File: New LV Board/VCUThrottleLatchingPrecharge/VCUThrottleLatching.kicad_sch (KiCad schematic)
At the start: 30 parts, among them J1 B12B-PH-K-S:JST_B12B-PH-K-S, Q1 SS8550, U1 IRLML2060TRPBF, U2 IRLML2060TRPBF, U3 IRLML2060TRPBF, U5 IRLML2060TRPBF, U6 IRLML2060TRPBF, U8 PMV160UP, U9 NE555D

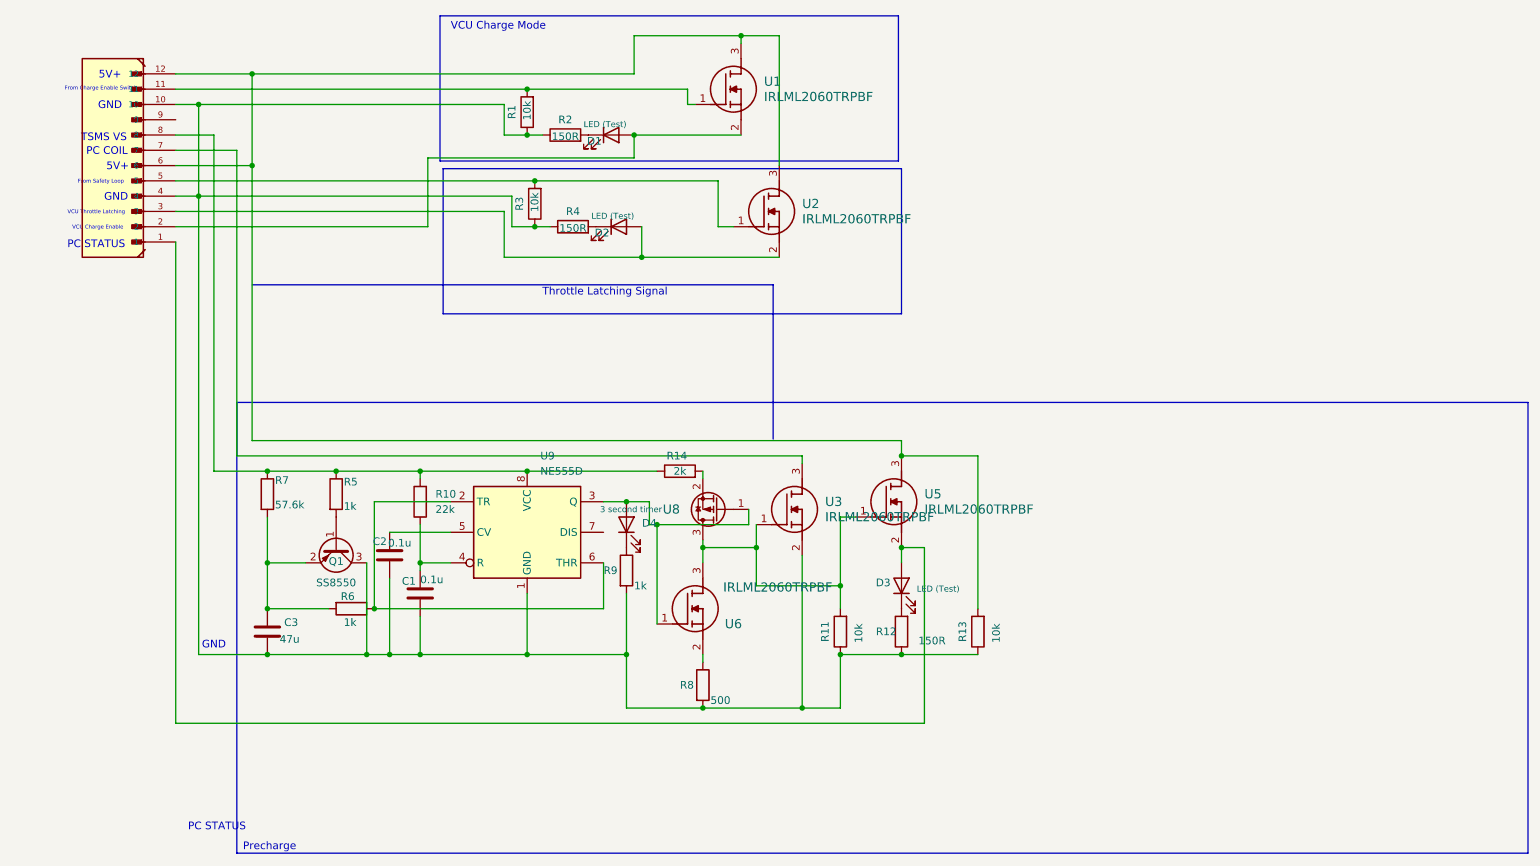
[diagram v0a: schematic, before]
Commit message: VCU Latch and Precharge Schematic Update + Footprint Adjustments
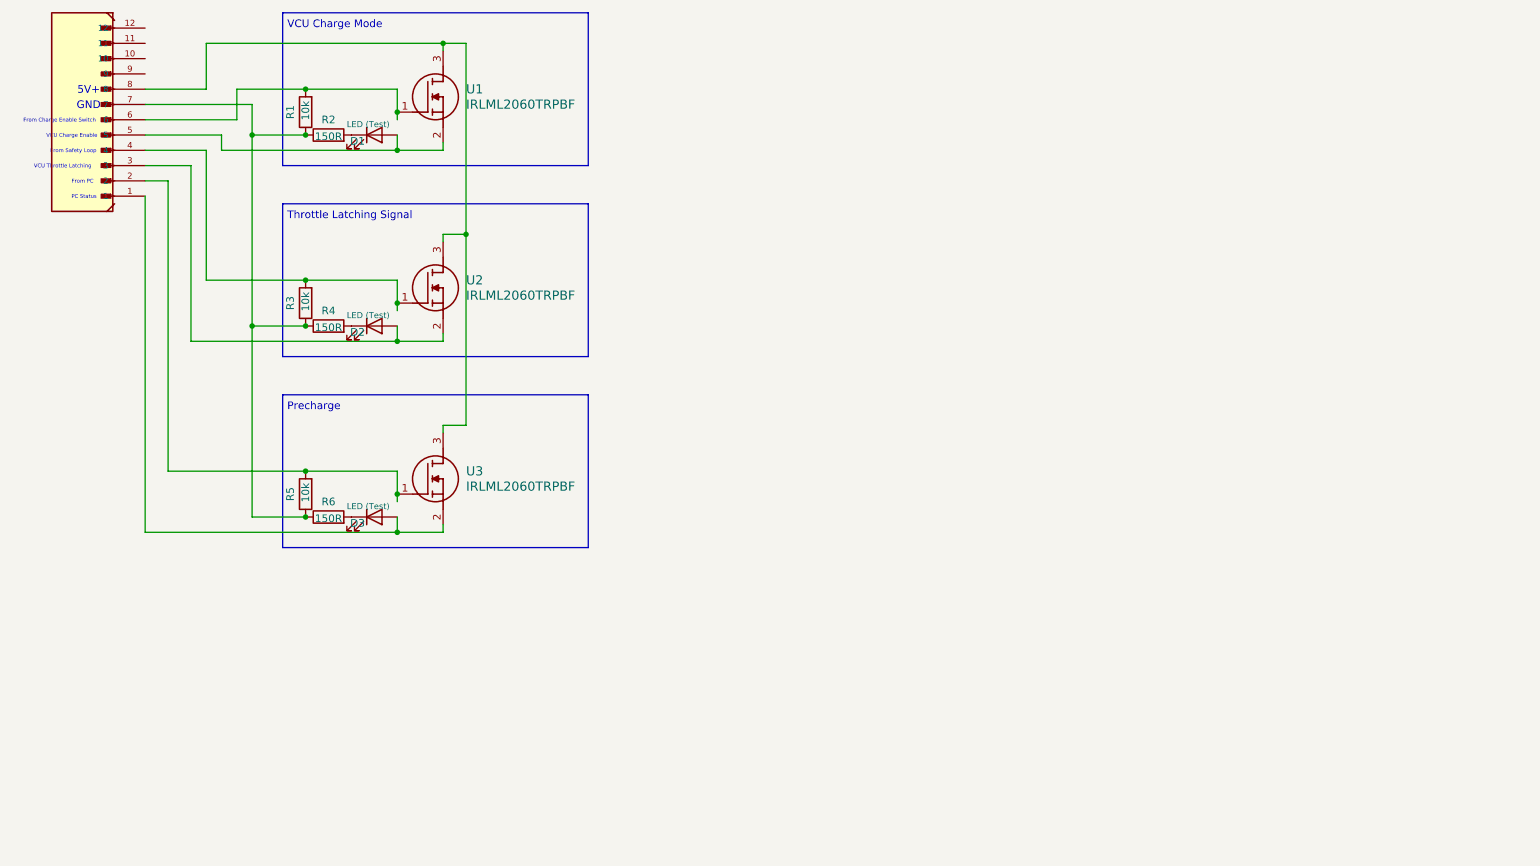
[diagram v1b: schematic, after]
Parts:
- removed C1: 0.1u, Capacitor_SMD:C_1206_3216Metric_Pad1.33x1.80mm_HandSolder, symbol Device:C
- removed C2: 0.1u, C_1206_3216Metric_Pad1.33x1.80mm_HandSolder, symbol Device:C
- removed C3: 47u, C_1206_3216Metric_Pad1.33x1.80mm_HandSolder, symbol Device:C
- removed D4: 3 second timer, LED_THT:LED_D3.0mm, symbol Device:LED
- removed Q1: SS8550, Footprints:SOT95P237X112-3N, symbol Transistor_BJT:SS8550
- removed R10: 22k, Footprints:STA_CF14_STP, symbol Device:R
- removed R11, R13: 10k, Footprints:STA_CF14_STP, symbol Device:R
- removed R12: 150R, Footprints:STA_CF14_STP, symbol Device:R
- removed R14: 2k, Footprints:STA_CF14_STP, symbol Device:R
- removed R7: 57.6k, Footprints:STA_CF14_STP, symbol Device:R
- removed R8: 500, Footprints:STA_CF14_STP, symbol Device:R
- removed R9: 1k, Footprints:STA_CF14_STP, symbol Device:R
- removed U5, U6: IRLML2060TRPBF, Package_TO_SOT_SMD:SOT-23-3, symbol IRLML2060TRPBF:IRLML2060TRPBF
- removed U8: PMV160UP, Package_TO_SOT_SMD:SOT-23-3, symbol Transistor_FET:Q_PMOS_GSD
- removed U9: NE555D, Footprints:SOIC127P599X175-8N, symbol Timer:NE555D
- R1, R2, R3, R4: footprint Footprints:STA_CF14_STP -> Resistor_THT:R_Axial_DIN0207_L6.3mm_D2.5mm_P10.16mm_Horizontal
- R5: value 1k -> 10k; footprint Footprints:STA_CF14_STP -> Resistor_THT:R_Axial_DIN0207_L6.3mm_D2.5mm_P10.16mm_Horizontal
- R6: value 1k -> 150R; footprint Footprints:STA_CF14_STP -> Resistor_THT:R_Axial_DIN0207_L6.3mm_D2.5mm_P10.16mm_Horizontal
- U1, U2, U3: footprint Package_TO_SOT_SMD:SOT-23-3 -> Motorsports:DPAK-3_6P35X6P73_ONS
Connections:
- net at D3.1 (K): now also R6.2
- net at D3.2 (A), J1.1: now also U3.2 (S)
- net at U3.1 (G): now also J1.2, R5.2
- net at R1.1, R2.1, R3.1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: now also J1.7, R5.1, R6.1; no longer J1.10, J1.4, U3.2 (S)
- net at R1.2, U1.1 (G): now also J1.6; no longer J1.11
- net at D1.2 (A), U1.2 (S): now also J1.5; no longer J1.2
- net at J1.8: now also U1.3 (D), U2.3 (D), U3.3 (D); no longer R5.1
- net at R3.2, U2.1 (G): now also J1.4; no longer J1.5
- now unconnected: J1.12
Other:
- note added: "From PC"
- note added: "PC Status"
- note removed: "PC COIL"
- note removed: "PC STATUS"
- note removed: "TSMS VS"
- moved on the sheet: D1, R1, R2, U1

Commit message: throttle lathcing done I hope
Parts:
- J1: footprint Connector_PinHeader_2.54mm:PinHeader_1x12_P2.54mm_Vertical -> Connector_JST:JST_PH_B12B-PH-K_1x12_P2.00mm_Vertical
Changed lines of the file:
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@@
 			)
 		)
-		(property "Footprint" "Connector_PinHeader_2.54mm:PinHeader_1x12_P2.54mm_Vertical"
+		(property "Footprint" "Connector_JST:JST_PH_B12B-PH-K_1x12_P2.00mm_Vertical"
 			(at 30.48 40.64 0)
 			(effects
